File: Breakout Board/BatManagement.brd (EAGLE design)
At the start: 95.6 x 70.4 mm, 23 parts, among them J1 RASPBERRYPI-40-PIN-GPIO_PTH, SW1 100SP1T2B4M6QE, X3 22-23-2031, X4 22-23-2031

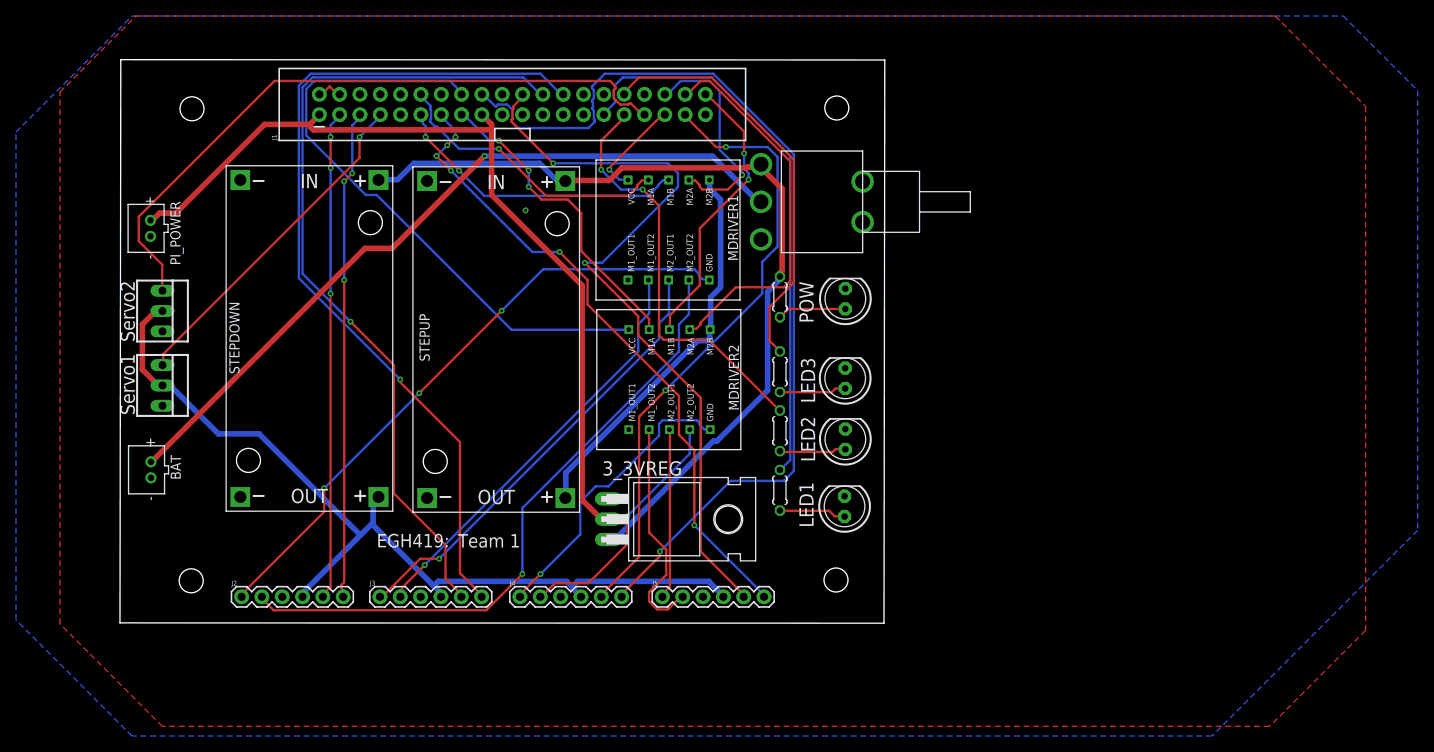
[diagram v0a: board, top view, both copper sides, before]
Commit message: Added jumper to breakout2
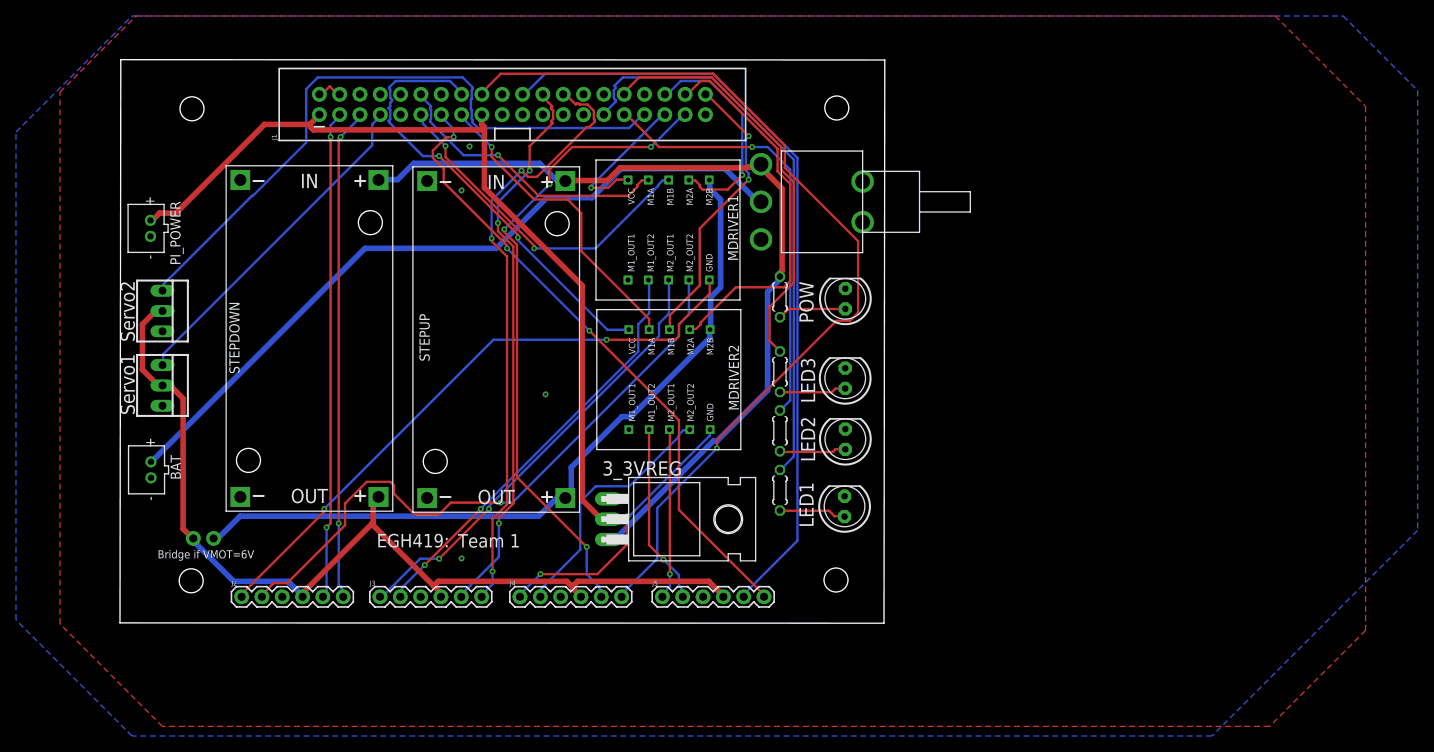
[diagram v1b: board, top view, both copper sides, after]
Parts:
- added J6: (no value), SparkFun-Connectors:1X02
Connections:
- net 5V: now also J6.2
- net VMOT: now also J6.1
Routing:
- net VMOT: track 49.0 -> 95.2 mm
- net ENC2A: track 103.4 -> 69.9 mm, vias 1 -> 3
- net ENC2B: track 108.2 -> 75.5 mm, vias 1 -> 3
- net M4B: track 76.8 -> 56.2 mm, vias 0 -> 2
- net 5V: track 113.6 -> 119.6 mm
- net M4_2: track 28.6 -> 22.6 mm, vias 0 -> 1
- net M1B: track 37.4 -> 43.0 mm
- net M2B: track 12.8 -> 18.2 mm
- net ENC3B: track 120.5 -> 116.3 mm
- net ENC4A: track 94.7 -> 97.5 mm, vias 2 -> 0
- net ENC3A: track 78.1 -> 80.6 mm, vias 2 -> 4
- net SERVO2: track 83.7 -> 81.7 mm
- net LED2: track 52.3 -> 54.3 mm, vias 2 -> 1
- net M3_1: track 37.0 -> 35.1 mm, vias 1 -> 2
- net M1_2: track 80.7 -> 78.9 mm
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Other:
- board text added: "Bridge if VMOT=6V"
